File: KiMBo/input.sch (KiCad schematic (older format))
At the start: 10 parts, among them P35 PWR_Input, Q3 IPD90P03P4-04

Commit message: Leave SPI0 free for a display, reassign pins so SPI1 is available
Fix some typos/errors
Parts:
- renumbered Q3 to Q4, R26 to R28
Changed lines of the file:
@@
 $EndComp
 $Comp
-L GND #PWR084
+L GND #PWR083
 U 1 1 57844140
 P 7150 5350
-F 0 "#PWR084" H 7150 5100 50  0001 C CNN
+F 0 "#PWR083" H 7150 5100 50  0001 C CNN
 F 1 "GND" H 7155 5177 50  0000 C CNN
 F 2 "" H 7150 5350 50  0000 C CNN
@@
 $EndComp
 $Comp
-L +24V #PWR085
+L +24V #PWR084
 U 1 1 578441AE
 P 9650 4350
-F 0 "#PWR085" H 9650 4200 50  0001 C CNN
+F 0 "#PWR084" H 9650 4200 50  0001 C CNN
 F 1 "+24V" H 9665 4523 50  0000 C CNN
 F 2 "" H 9650 4350 50  0000 C CNN
@@
 $EndComp
 $Comp
-L PWR_FLAG #FLG086
+L PWR_FLAG #FLG085
 U 1 1 578C3A54
 P 9350 4350
-F 0 "#FLG086" H 9350 4445 50  0001 C CNN
+F 0 "#FLG085" H 9350 4445 50  0001 C CNN
 F 1 "PWR_FLAG" H 9350 4574 50  0000 C CNN
 F 2 "" H 9350 4350 50  0000 C CNN
@@
 $EndComp
 $Comp
-L CGND #PWR087
+L CGND #PWR086
 U 1 1 5B0EE826
 P 7650 5350
-F 0 "#PWR087" H 7650 5150 50  0001 C CNN
+F 0 "#PWR086" H 7650 5150 50  0001 C CNN
 F 1 "CGND" H 7650 5200 50  0000 C CNN
 F 2 "" H 7650 5300 50  0000 C CNN
@@
 $EndComp
 $Comp
-L PWR_FLAG #FLG088
+L PWR_FLAG #FLG087
 U 1 1 5B0EECCD
 P 7400 5250
-F 0 "#FLG088" H 7400 5345 50  0001 C CNN
+F 0 "#FLG087" H 7400 5345 50  0001 C CNN
 F 1 "PWR_FLAG" H 7400 5474 50  0000 C CNN
 F 2 "" H 7400 5250 50  0000 C CNN
@@
 $EndComp
 $Comp
-L GND #PWR089
+L GND #PWR088
 U 1 1 5B10C925
 P 9350 4950
-F 0 "#PWR089" H 9350 4700 50  0001 C CNN
+F 0 "#PWR088" H 9350 4700 50  0001 C CNN
 F 1 "GND" H 9355 4777 50  0000 C CNN
 F 2 "" H 9350 4950 50  0000 C CNN
@@
 $EndComp
 $Comp
-L DMP3098L-7 Q3
+L DMP3098L-7 Q4
 U 1 1 5B62E149
 P 7950 4500
-F 0 "Q3" V 8275 4450 50  0000 L CNN
+F 0 "Q4" V 8275 4450 50  0000 L CNN
 F 1 "IPD90P03P4-04" V 8175 4200 50  0000 L CNN
 F 2 "" H 8200 4575 50  0001 L CNN
@@
 $EndComp
 $Comp
-L R R26
+L R R28
 U 1 1 5B62F66A
 P 7950 5100
-F 0 "R26" H 8020 5146 50  0000 L CNN
+F 0 "R28" H 8020 5146 50  0000 L CNN
 F 1 "100kΩ" H 8020 5055 50  0000 L CNN
 F 2 "" V 7880 5100 50  0001 C CNN

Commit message: Use fixed 5V LM2592HV Buck, include SPI0 header for LCD
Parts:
- renumbered C13 to C10, C14 to C11, FB17 to FB22, FB18 to FB23, P35 to P36, R28 to R25
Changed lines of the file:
@@
 $EndComp
 $Comp
-L GND #PWR083
+L GND #PWR078
 U 1 1 57844140
 P 7150 5350
-F 0 "#PWR083" H 7150 5100 50  0001 C CNN
+F 0 "#PWR078" H 7150 5100 50  0001 C CNN
 F 1 "GND" H 7155 5177 50  0000 C CNN
 F 2 "" H 7150 5350 50  0000 C CNN
@@
 $EndComp
 $Comp
-L C C13
+L C C10
 U 1 1 5784416E
 P 9350 4650
-F 0 "C13" H 9400 4750 50  0000 L CNN
+F 0 "C10" H 9400 4750 50  0000 L CNN
 F 1 "22μF" H 9400 4550 50  0000 L CNN
 F 2 "Capacitors_SMD:C_0805" H 9388 4500 50  0001 C CNN
@@
 $EndComp
 $Comp
-L C C14
+L C C11
 U 1 1 57844175
 P 9650 4650
-F 0 "C14" H 9700 4750 50  0000 L CNN
+F 0 "C11" H 9700 4750 50  0000 L CNN
 F 1 "22μF" H 9700 4550 50  0000 L CNN
 F 2 "Capacitors_SMD:C_0805" H 9688 4500 50  0001 C CNN
@@
 $EndComp
 $Comp
-L +24V #PWR084
+L +24V #PWR079
 U 1 1 578441AE
 P 9650 4350
-F 0 "#PWR084" H 9650 4200 50  0001 C CNN
+F 0 "#PWR079" H 9650 4200 50  0001 C CNN
 F 1 "+24V" H 9665 4523 50  0000 C CNN
 F 2 "" H 9650 4350 50  0000 C CNN
@@
 $EndComp
 $Comp
-L CONN_01X04 P35
+L CONN_01X04 P36
 U 1 1 57844205
 P 6900 4550
-F 0 "P35" H 6978 4591 50  0000 L CNN
+F 0 "P36" H 6978 4591 50  0000 L CNN
 F 1 "PWR_Input" H 6978 4500 50  0000 L CNN
 F 2 "" H 6900 4550 50  0001 C CNN
@@
 $EndComp
 $Comp
-L PWR_FLAG #FLG085
+L PWR_FLAG #FLG080
 U 1 1 578C3A54
 P 9350 4350
-F 0 "#FLG085" H 9350 4445 50  0001 C CNN
+F 0 "#FLG080" H 9350 4445 50  0001 C CNN
 F 1 "PWR_FLAG" H 9350 4574 50  0000 C CNN
 F 2 "" H 9350 4350 50  0000 C CNN
@@
 $EndComp
 $Comp
-L CGND #PWR086
+L CGND #PWR081
 U 1 1 5B0EE826
 P 7650 5350
-F 0 "#PWR086" H 7650 5150 50  0001 C CNN
+F 0 "#PWR081" H 7650 5150 50  0001 C CNN
 F 1 "CGND" H 7650 5200 50  0000 C CNN
 F 2 "" H 7650 5300 50  0000 C CNN
@@
 $EndComp
 $Comp
-L PWR_FLAG #FLG087
+L PWR_FLAG #FLG082
 U 1 1 5B0EECCD
 P 7400 5250
-F 0 "#FLG087" H 7400 5345 50  0001 C CNN
+F 0 "#FLG082" H 7400 5345 50  0001 C CNN
 F 1 "PWR_FLAG" H 7400 5474 50  0000 C CNN
 F 2 "" H 7400 5250 50  0000 C CNN
@@
 $EndComp
 $Comp
-L GND #PWR088
+L GND #PWR083
 U 1 1 5B10C925
 P 9350 4950
-F 0 "#PWR088" H 9350 4700 50  0001 C CNN
+F 0 "#PWR083" H 9350 4700 50  0001 C CNN
 F 1 "GND" H 9355 4777 50  0000 C CNN
 F 2 "" H 9350 4950 50  0000 C CNN
@@
 $EndComp
 $Comp
-L INDUCTOR_Small FB17
+L INDUCTOR_Small FB22
 U 1 1 5B625E79
 P 8650 4350
-F 0 "FB17" V 8835 4350 50  0000 C CNN
+F 0 "FB22" V 8835 4350 50  0000 C CNN
 F 1 "BLM31SN500SN1L" V 8744 4350 50  0000 C CNN
 F 2 "" H 8650 4350 50  0001 C CNN
@@
 $EndComp
 $Comp
-L INDUCTOR_Small FB18
+L INDUCTOR_Small FB23
 U 1 1 5B625E80
 P 8650 4450
-F 0 "FB18" V 8835 4450 50  0000 C CNN
+F 0 "FB23" V 8835 4450 50  0000 C CNN
 F 1 "BLM31SN500SN1L" V 8744 4450 50  0000 C CNN
 F 2 "" H 8650 4450 50  0001 C CNN
@@
 $EndComp
 $Comp
-L R R28
+L R R25
 U 1 1 5B62F66A
 P 7950 5100
-F 0 "R28" H 8020 5146 50  0000 L CNN
+F 0 "R25" H 8020 5146 50  0000 L CNN
 F 1 "100kΩ" H 8020 5055 50  0000 L CNN
 F 2 "" V 7880 5100 50  0001 C CNN

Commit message: Assocate more footprints
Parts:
- FB22, FB23: footprint (none) -> Resistors_SMD:R_1206_HandSoldering
- R25: footprint (none) -> Resistors_SMD:R_0603
- renumbered D12 to D13, D13 to D14
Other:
- note added: "refer to\nlanding pattern!"
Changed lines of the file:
@@
 $EndComp
 $Comp
-L ZENER D13
+L ZENER D14
 U 1 1 578CA60C
 P 9050 4650
-F 0 "D13" V 9050 4450 50  0000 C CNN
+F 0 "D14" V 9050 4450 50  0000 C CNN
 F 1 "SMAJ26A" V 9150 4450 50  0000 C CNN
 F 2 "" H 9050 4650 50  0001 C CNN
@@
 F 0 "FB22" V 8835 4350 50  0000 C CNN
 F 1 "BLM31SN500SN1L" V 8744 4350 50  0000 C CNN
-F 2 "" H 8650 4350 50  0001 C CNN
+F 2 "Resistors_SMD:R_1206_HandSoldering" H 8650 4350 50  0001 C CNN
 F 3 "" H 8650 4350 50  0000 C CNN
 	1    8650 4350
@@
 F 0 "FB23" V 8835 4450 50  0000 C CNN
 F 1 "BLM31SN500SN1L" V 8744 4450 50  0000 C CNN
-F 2 "" H 8650 4450 50  0001 C CNN
+F 2 "Resistors_SMD:R_1206_HandSoldering" H 8650 4450 50  0001 C CNN
 F 3 "" H 8650 4450 50  0000 C CNN
 	1    8650 4450
@@
 $EndComp
 $Comp
-L ZENER D12
+L ZENER D13
 U 1 1 5B62F4CA
 P 8250 4650
-F 0 "D12" V 8250 4550 50  0000 R CNN
+F 0 "D13" V 8250 4550 50  0000 R CNN
 F 1 "SMAZ10" V 8350 4600 50  0000 R CNN
 F 2 "" H 8250 4650 50  0001 C CNN
@@
 F 0 "R25" H 8020 5146 50  0000 L CNN
 F 1 "100kΩ" H 8020 5055 50  0000 L CNN
-F 2 "" V 7880 5100 50  0001 C CNN
+F 2 "Resistors_SMD:R_0603" V 7880 5100 50  0001 C CNN
 F 3 "" H 7950 5100 50  0000 C CNN
 	1    7950 5100
 	1    0    0    -1
 $EndComp
-Text Notes 8150 4050 0    60   ~ 0
+Text Notes 8150 3850 0    60   ~ 0
 Inductors in parallel\nin order to handle the current\n*half the impedance*
 Text Notes 6700 4200 0    60   ~ 0
@@
 	7650 5350 7650 5300
 Connection ~ 7650 5300
+Text Notes 8250 4050 0    60   ~ 0
+    refer to\nlanding pattern!
 $EndSCHEMATC

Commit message: More footprint association
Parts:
- D14: renamed from D13; footprint (none) -> KiMBo:SMA-DO-214AC
- D15: renamed from D14; footprint (none) -> KiMBo:SK-DO-214AC
- P36: footprint (none) -> KiMBo:euro_header_4_angled
- Q4: footprint (none) -> TO_SOT_Packages_SMD:TO-252-2Lead
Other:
- note added: "39532-1004"
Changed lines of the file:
@@
 $EndComp
 $Comp
-L GND #PWR078
+L GND #PWR079
 U 1 1 57844140
 P 7150 5350
-F 0 "#PWR078" H 7150 5100 50  0001 C CNN
+F 0 "#PWR079" H 7150 5100 50  0001 C CNN
 F 1 "GND" H 7155 5177 50  0000 C CNN
 F 2 "" H 7150 5350 50  0000 C CNN
@@
 $EndComp
 $Comp
-L +24V #PWR079
+L +24V #PWR080
 U 1 1 578441AE
 P 9650 4350
-F 0 "#PWR079" H 9650 4200 50  0001 C CNN
+F 0 "#PWR080" H 9650 4200 50  0001 C CNN
 F 1 "+24V" H 9665 4523 50  0000 C CNN
 F 2 "" H 9650 4350 50  0000 C CNN
@@
 F 0 "P36" H 6978 4591 50  0000 L CNN
 F 1 "PWR_Input" H 6978 4500 50  0000 L CNN
-F 2 "" H 6900 4550 50  0001 C CNN
+F 2 "KiMBo:euro_header_4_angled" H 6900 4550 50  0001 C CNN
 F 3 "" H 6900 4550 50  0000 C CNN
 	1    6900 4550
@@
 $EndComp
 $Comp
-L PWR_FLAG #FLG080
+L PWR_FLAG #FLG081
 U 1 1 578C3A54
 P 9350 4350
-F 0 "#FLG080" H 9350 4445 50  0001 C CNN
+F 0 "#FLG081" H 9350 4445 50  0001 C CNN
 F 1 "PWR_FLAG" H 9350 4574 50  0000 C CNN
 F 2 "" H 9350 4350 50  0000 C CNN
@@
 $EndComp
 $Comp
-L ZENER D14
+L ZENER D15
 U 1 1 578CA60C
 P 9050 4650
-F 0 "D14" V 9050 4450 50  0000 C CNN
+F 0 "D15" V 9050 4450 50  0000 C CNN
 F 1 "SMAJ26A" V 9150 4450 50  0000 C CNN
-F 2 "" H 9050 4650 50  0001 C CNN
+F 2 "KiMBo:SK-DO-214AC" H 9050 4650 50  0001 C CNN
 F 3 "" H 9050 4650 50  0000 C CNN
 	1    9050 4650
@@
 $EndComp
 $Comp
-L CGND #PWR081
+L CGND #PWR082
 U 1 1 5B0EE826
 P 7650 5350
-F 0 "#PWR081" H 7650 5150 50  0001 C CNN
+F 0 "#PWR082" H 7650 5150 50  0001 C CNN
 F 1 "CGND" H 7650 5200 50  0000 C CNN
 F 2 "" H 7650 5300 50  0000 C CNN
@@
 $EndComp
 $Comp
-L PWR_FLAG #FLG082
+L PWR_FLAG #FLG083
 U 1 1 5B0EECCD
 P 7400 5250
-F 0 "#FLG082" H 7400 5345 50  0001 C CNN
+F 0 "#FLG083" H 7400 5345 50  0001 C CNN
 F 1 "PWR_FLAG" H 7400 5474 50  0000 C CNN
 F 2 "" H 7400 5250 50  0000 C CNN
@@
 $EndComp
 $Comp
-L GND #PWR083
+L GND #PWR084
 U 1 1 5B10C925
 P 9350 4950
-F 0 "#PWR083" H 9350 4700 50  0001 C CNN
+F 0 "#PWR084" H 9350 4700 50  0001 C CNN
 F 1 "GND" H 9355 4777 50  0000 C CNN
 F 2 "" H 9350 4950 50  0000 C CNN
@@
 F 0 "Q4" V 8275 4450 50  0000 L CNN
 F 1 "IPD90P03P4-04" V 8175 4200 50  0000 L CNN
-F 2 "" H 8200 4575 50  0001 L CNN
+F 2 "TO_SOT_Packages_SMD:TO-252-2Lead" H 8200 4575 50  0001 L CNN
 F 3 "http://aosmd.com/res/data_sheets/AOD417.pdf" H 8141 4409 50  0001 L CNN
 	1    7950 4500
@@
 $EndComp
 $Comp
-L ZENER D13
+L ZENER D14
 U 1 1 5B62F4CA
 P 8250 4650
-F 0 "D13" V 8250 4550 50  0000 R CNN
+F 0 "D14" V 8250 4550 50  0000 R CNN
 F 1 "SMAZ10" V 8350 4600 50  0000 R CNN
-F 2 "" H 8250 4650 50  0001 C CNN
+F 2 "KiMBo:SMA-DO-214AC" H 8250 4650 50  0001 C CNN
 F 3 "" H 8250 4650 50  0000 C CNN
 	1    8250 4650
@@
 Text Notes 8250 4050 0    60   ~ 0
     refer to\nlanding pattern!
+Text Notes 6200 4400 0    60   ~ 0
+39532-1004
 $EndSCHEMATC

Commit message: Create more footprints and add more associations
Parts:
- F1: footprint (none) -> KiMBo:3557-2-Fuseholder
- renumbered P36 to P38
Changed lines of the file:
@@
 F 0 "F1" H 7450 4550 50  0000 C CNN
 F 1 "0891020.NXS" H 7450 4250 50  0000 C CNN
-F 2 "" H 7450 4400 50  0001 C CNN
+F 2 "KiMBo:3557-2-Fuseholder" H 7450 4400 50  0001 C CNN
 F 3 "" H 7450 4400 50  0000 C CNN
 	1    7450 4400
@@
 $EndComp
 $Comp
-L CONN_01X04 P36
+L CONN_01X04 P38
 U 1 1 57844205
 P 6900 4550
-F 0 "P36" H 6978 4591 50  0000 L CNN
+F 0 "P38" H 6978 4591 50  0000 L CNN
 F 1 "PWR_Input" H 6978 4500 50  0000 L CNN
 F 2 "KiMBo:euro_header_4_angled" H 6900 4550 50  0001 C CNN

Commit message: Begin layout
Arrange all connectors to get a feel for the area.
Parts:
- renumbered C10 to C12, C11 to C13, D14 to D15, D15 to D16, P38 to P37
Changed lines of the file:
@@
 $EndComp
 $Comp
-L GND #PWR079
+L GND #PWR082
 U 1 1 57844140
 P 7150 5350
-F 0 "#PWR079" H 7150 5100 50  0001 C CNN
+F 0 "#PWR082" H 7150 5100 50  0001 C CNN
 F 1 "GND" H 7155 5177 50  0000 C CNN
 F 2 "" H 7150 5350 50  0000 C CNN
@@
 $EndComp
 $Comp
-L C C10
+L C C12
 U 1 1 5784416E
 P 9350 4650
-F 0 "C10" H 9400 4750 50  0000 L CNN
+F 0 "C12" H 9400 4750 50  0000 L CNN
 F 1 "22μF" H 9400 4550 50  0000 L CNN
 F 2 "Capacitors_SMD:C_0805" H 9388 4500 50  0001 C CNN
@@
 $EndComp
 $Comp
-L C C11
+L C C13
 U 1 1 57844175
 P 9650 4650
-F 0 "C11" H 9700 4750 50  0000 L CNN
+F 0 "C13" H 9700 4750 50  0000 L CNN
 F 1 "22μF" H 9700 4550 50  0000 L CNN
 F 2 "Capacitors_SMD:C_0805" H 9688 4500 50  0001 C CNN
@@
 $EndComp
 $Comp
-L +24V #PWR080
+L +24V #PWR083
 U 1 1 578441AE
 P 9650 4350
-F 0 "#PWR080" H 9650 4200 50  0001 C CNN
+F 0 "#PWR083" H 9650 4200 50  0001 C CNN
 F 1 "+24V" H 9665 4523 50  0000 C CNN
 F 2 "" H 9650 4350 50  0000 C CNN
@@
 $EndComp
 $Comp
-L CONN_01X04 P38
+L CONN_01X04 P37
 U 1 1 57844205
 P 6900 4550
-F 0 "P38" H 6978 4591 50  0000 L CNN
+F 0 "P37" H 6978 4591 50  0000 L CNN
 F 1 "PWR_Input" H 6978 4500 50  0000 L CNN
 F 2 "KiMBo:euro_header_4_angled" H 6900 4550 50  0001 C CNN
@@
 $EndComp
 $Comp
-L PWR_FLAG #FLG081
+L PWR_FLAG #FLG084
 U 1 1 578C3A54
 P 9350 4350
-F 0 "#FLG081" H 9350 4445 50  0001 C CNN
+F 0 "#FLG084" H 9350 4445 50  0001 C CNN
 F 1 "PWR_FLAG" H 9350 4574 50  0000 C CNN
 F 2 "" H 9350 4350 50  0000 C CNN
@@
 $EndComp
 $Comp
-L ZENER D15
+L ZENER D16
 U 1 1 578CA60C
 P 9050 4650
-F 0 "D15" V 9050 4450 50  0000 C CNN
+F 0 "D16" V 9050 4450 50  0000 C CNN
 F 1 "SMAJ26A" V 9150 4450 50  0000 C CNN
 F 2 "KiMBo:SK-DO-214AC" H 9050 4650 50  0001 C CNN
@@
 $EndComp
 $Comp
-L CGND #PWR082
-U 1 1 5B0EE826
-P 7650 5350
-F 0 "#PWR082" H 7650 5150 50  0001 C CNN
-F 1 "CGND" H 7650 5200 50  0000 C CNN
-F 2 "" H 7650 5300 50  0000 C CNN
-F 3 "" H 7650 5300 50  0000 C CNN
-	1    7650 5350
-	1    0    0    -1
-$EndComp
-$Comp
-L PWR_FLAG #FLG083
+L PWR_FLAG #FLG085
 U 1 1 5B0EECCD
 P 7400 5250
-F 0 "#FLG083" H 7400 5345 50  0001 C CNN
+F 0 "#FLG085" H 7400 5345 50  0001 C CNN
 F 1 "PWR_FLAG" H 7400 5474 50  0000 C CNN
 F 2 "" H 7400 5250 50  0000 C CNN
@@
 $EndComp
 $Comp
-L GND #PWR084
+L GND #PWR086
 U 1 1 5B10C925
 P 9350 4950
-F 0 "#PWR084" H 9350 4700 50  0001 C CNN
+F 0 "#PWR086" H 9350 4700 50  0001 C CNN
 F 1 "GND" H 9355 4777 50  0000 C CNN
 F 2 "" H 9350 4950 50  0000 C CNN
@@
 $EndComp
 $Comp
-L ZENER D14
+L ZENER D15
 U 1 1 5B62F4CA
 P 8250 4650
-F 0 "D14" V 8250 4550 50  0000 R CNN
+F 0 "D15" V 8250 4550 50  0000 R CNN
 F 1 "SMAZ10" V 8350 4600 50  0000 R CNN
 F 2 "KiMBo:SMA-DO-214AC" H 8250 4650 50  0001 C CNN
@@
 Text Notes 6200 4400 0    60   ~ 0
 39532-1004
+$Comp
+L CGND #PWR087
+U 1 1 5904D2A9
+P 7650 5350
+F 0 "#PWR087" H 7650 5150 50  0001 C CNN
+F 1 "CGND" H 7650 5200 50  0000 C CNN
+F 2 "" H 7650 5300 50  0000 C CNN
+F 3 "" H 7650 5300 50  0000 C CNN
+	1    7650 5350
+	1    0    0    -1
+$EndComp
 $EndSCHEMATC

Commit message: Remove HDMI from the schematic
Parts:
- renumbered P37 to P36
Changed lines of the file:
@@
 $Descr A3 16535 11693
 encoding utf-8
-Sheet 4 26
+Sheet 4 25
 Title ""
 Date ""
@@
 $EndComp
 $Comp
-L GND #PWR082
+L GND #PWR080
 U 1 1 57844140
 P 7150 5350
-F 0 "#PWR082" H 7150 5100 50  0001 C CNN
+F 0 "#PWR080" H 7150 5100 50  0001 C CNN
 F 1 "GND" H 7155 5177 50  0000 C CNN
 F 2 "" H 7150 5350 50  0000 C CNN
@@
 $EndComp
 $Comp
-L +24V #PWR083
+L +24V #PWR081
 U 1 1 578441AE
 P 9650 4350
-F 0 "#PWR083" H 9650 4200 50  0001 C CNN
+F 0 "#PWR081" H 9650 4200 50  0001 C CNN
 F 1 "+24V" H 9665 4523 50  0000 C CNN
 F 2 "" H 9650 4350 50  0000 C CNN
@@
 $EndComp
 $Comp
-L CONN_01X04 P37
+L CONN_01X04 P36
 U 1 1 57844205
 P 6900 4550
-F 0 "P37" H 6978 4591 50  0000 L CNN
+F 0 "P36" H 6978 4591 50  0000 L CNN
 F 1 "PWR_Input" H 6978 4500 50  0000 L CNN
 F 2 "KiMBo:euro_header_4_angled" H 6900 4550 50  0001 C CNN
@@
 $EndComp
 $Comp
-L PWR_FLAG #FLG084
+L PWR_FLAG #FLG082
 U 1 1 578C3A54
 P 9350 4350
-F 0 "#FLG084" H 9350 4445 50  0001 C CNN
+F 0 "#FLG082" H 9350 4445 50  0001 C CNN
 F 1 "PWR_FLAG" H 9350 4574 50  0000 C CNN
 F 2 "" H 9350 4350 50  0000 C CNN
@@
 $EndComp
 $Comp
-L PWR_FLAG #FLG085
+L PWR_FLAG #FLG083
 U 1 1 5B0EECCD
 P 7400 5250
-F 0 "#FLG085" H 7400 5345 50  0001 C CNN
+F 0 "#FLG083" H 7400 5345 50  0001 C CNN
 F 1 "PWR_FLAG" H 7400 5474 50  0000 C CNN
 F 2 "" H 7400 5250 50  0000 C CNN
@@
 $EndComp
 $Comp
-L GND #PWR086
+L GND #PWR084
 U 1 1 5B10C925
 P 9350 4950
-F 0 "#PWR086" H 9350 4700 50  0001 C CNN
+F 0 "#PWR084" H 9350 4700 50  0001 C CNN
 F 1 "GND" H 9355 4777 50  0000 C CNN
 F 2 "" H 9350 4950 50  0000 C CNN
@@
 39532-1004
 $Comp
-L CGND #PWR087
+L CGND #PWR085
 U 1 1 5904D2A9
 P 7650 5350
-F 0 "#PWR087" H 7650 5150 50  0001 C CNN
+F 0 "#PWR085" H 7650 5150 50  0001 C CNN
 F 1 "CGND" H 7650 5200 50  0000 C CNN
 F 2 "" H 7650 5300 50  0000 C CNN

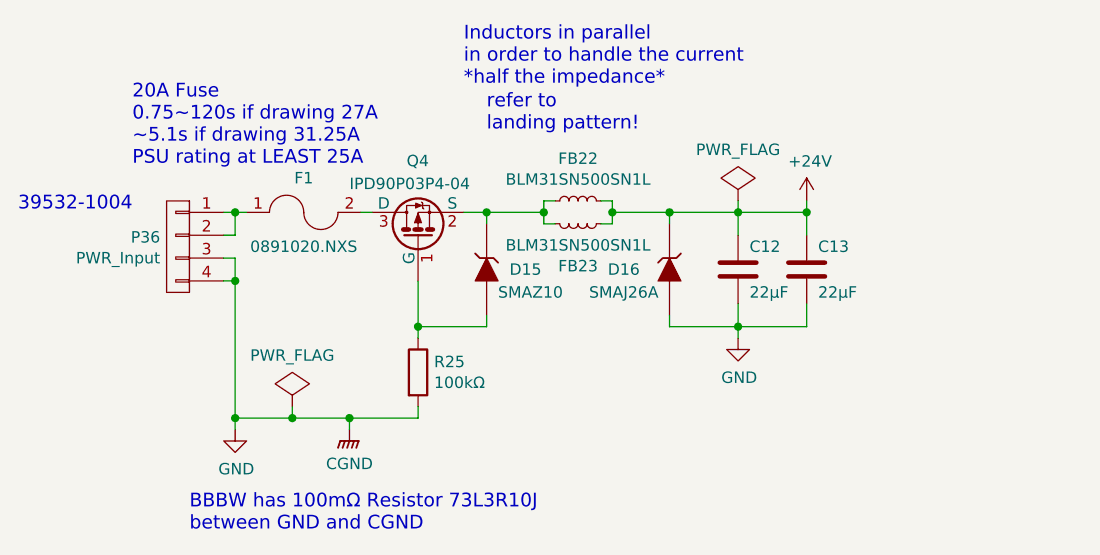
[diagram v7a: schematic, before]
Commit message: Complete stepper footprint association, move silkscreen, start DC fuse, polarity protection, and circuit
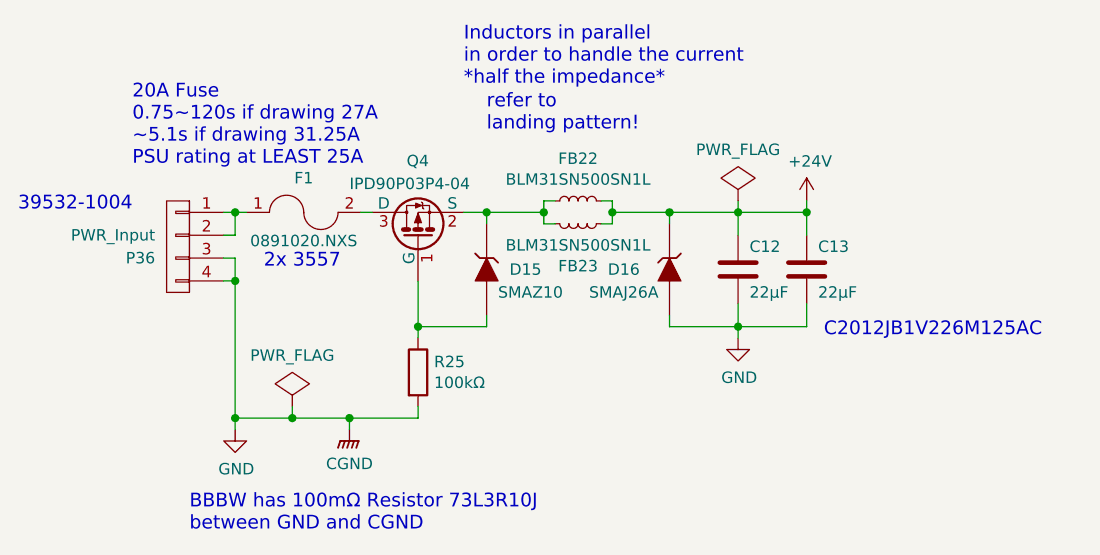
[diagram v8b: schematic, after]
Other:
- note added: "2x 3557"
- note added: "C2012JB1V226M125AC"
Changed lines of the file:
@@
 P 7450 4400
 F 0 "F1" H 7450 4550 50  0000 C CNN
-F 1 "0891020.NXS" H 7450 4250 50  0000 C CNN
+F 1 "0891020.NXS" H 7450 4275 50  0000 C CNN
 F 2 "KiMBo:3557-2-Fuseholder" H 7450 4400 50  0001 C CNN
 F 3 "" H 7450 4400 50  0000 C CNN
@@
 U 1 1 57844205
 P 6900 4550
-F 0 "P36" H 6978 4591 50  0000 L CNN
-F 1 "PWR_Input" H 6978 4500 50  0000 L CNN
+F 0 "P36" H 7000 4500 50  0000 L CNN
+F 1 "PWR_Input" H 7000 4600 50  0000 L CNN
 F 2 "KiMBo:euro_header_4_angled" H 6900 4550 50  0001 C CNN
 F 3 "" H 6900 4550 50  0000 C CNN
@@
 	1    0    0    -1
 $EndComp
+Text Notes 7275 4650 0    60   ~ 0
+2x 3557
+Text Notes 9725 4950 0    60   ~ 0
+C2012JB1V226M125AC
 $EndSCHEMATC
